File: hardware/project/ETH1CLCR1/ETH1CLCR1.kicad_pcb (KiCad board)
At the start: 6 copper layers, 160 x 100 mm, 680 parts, among them J1101 Conn_02x05, J1601 C64AC, J301 Conn_02x05, J302 Conn_02x01, J901 Conn_02x05, K1001 9012, K1002 9012, K1003 9012, K1004 9012, K1201 TQ2SA-5V, K1601 HE3621A0510, K1602 HE3621A0510, K1603 HE3621A0510, K1604 HE3621A0510, K1605 HE3621A0510, K1606 HE3621A0510, Q1001 MMBT4401L, Q1002 MMBT4403L, Q1003 BC847W, Q1004 BC847W, Q1005 BC847W, Q1006 BC847W, Q1201 2N2218A, Q1202 BC847W, Q1203 2N2904A, Q1204 BC847W, Q1501 BC847, Q1502 BC847, Q1503 BC847, Q1504 BC847, Q501 IRFR5410, U1001 TL072, U1002 LT1468, U1003 AQY212GS, U1004 AD5293BRUZ-20, U1101 STM32H743ZI, U1102 24LC08B-E/MS, U1201 AQY212GS, U1202 AQY212GS, U1203 AD5293BRUZ-20, U1204 TL072, U1205 AQY212GS, U1206 AQY212GS, U1207 AQY212GS, U1208 AQY212GS, U1209 AQY212GS, U1210 AQY212GS, U1211 AQY212GS, U1212 AQY212GS, U1213 HA3-2525-5Z, U1214 AQY212GS, U1215 AQY212GS, U1301 AQY212GS, U1302 TL072, U1303 AQY212GS, U1304 TL072, U1305 AQY212GS, U1306 AQY212GS, U1307 TL071, U1308 AQY212GS, U1309 TL072, U1310 AQY212GS, U1311 AQY212GS, U1312 TL072, U1313 AQY212GS, U1314 AQY212GS, U1315 TL071, U1316 AQY212GS, U1401 TL074, U1402 TL074, U1403 REF192, U1404 DAC7568ICPWR, U1501 INA159, U1502 ADG419BR, U1503 PGA103, U1504 OPA602, U1505 ADS8363, U1506 INA159, U1507 ADG419BR, U1508 PGA103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

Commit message: PCB layout
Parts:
- added C1218: C, Capacitor_SMD:C_0603_1608Metric_Pad1.05x0.95mm_HandSolder, B.Cu at (166.5, 51.8)
- C1206, C1208, C1209, C1210, C1211, C1212, C601, C602, C603, C604, C607, C613, C619, C620, C626, C901, C902, C903, C904, D1203, D1205, D1206, Q1202, R1216, R1217, R1219, R1220, R1222, R1223, R1224, R1225, R1226, R1227, R1229, R1230, R1231, R1234, R1238, R1239, R1242, R901, U1202, U1206, U1208, U1209, U1212, Y901: moved to B.Cu
- U602: value MC78M15CDTRKG -> MC7815BD2TG; footprint Package_TO_SOT_SMD:TO-252-2 -> Package_TO_SOT_SMD:TO-263-2
- U608: value MC79M15BDTRKG -> MC7915BD2TG; footprint Package_TO_SOT_SMD:TO-252-2 -> Package_TO_SOT_SMD:TO-263-2
- moved U1403 221.9 mm to (155.1, 98.7)
- moved Q1204 215.4 mm to (219.7, 79.6), turned to 270 degrees
- moved U1404 214.5 mm to (163.2, 98.7)
- moved U1212 212.4 mm to (186.1, 79.6), turned to 90 degrees
- moved K1201 211.7 mm to (199.5, 74.7), turned to 270 degrees
- moved C1206 207.4 mm to (193.2, 79.6), turned to 270 degrees
- moved U1207 206.9 mm to (186.1, 74.2), turned to 270 degrees
- moved U1214 203.9 mm to (209.7, 78.1)
- moved U1402 202.7 mm to (179.7, 97.0)
- moved U1205 201.6 mm to (186.2, 68.7), turned to 270 degrees
- moved R1214 200.8 mm to (190.8, 74.2), turned to 270 degrees
- moved R1216 200.3 mm to (209.7, 78.4), turned to 180 degrees
- moved R1215 198.5 mm to (181.4, 74.2), turned to 270 degrees
- moved U1210 196.4 mm to (215.6, 78.0)
- moved U1401 195.7 mm to (171.3, 97.0)
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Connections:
- C1006 pad 1: +12VF -> +15VF
- C1007 pad 1: +12VF -> +15VF
- C1008 pad 1: -12VF -> -15VF
- C1009 pad 1: -12VF -> -15VF
- U1001 pad 4: -12VF -> -15VF
- U1001 pad 8: +12VF -> +15VF

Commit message: PCB layout
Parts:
- removed the C801 at (161.1, 4.06)
- removed the C802 at (133.3, 29.8)
- removed the C818 at (136.1, 18.5)
- removed the C819 at (141.9, 15.2)
- removed the C820 at (141.9, 12.7)
- removed the C821 at (124.6, 30.6)
- removed the C822 at (152.4, 4.06)
- removed the C823 at (148.7, 6.57)
- removed the C824 at (131.9, 24.8)
- removed the C827 at (123.4, 33.1)
- removed the C828 at (144.2, 8.38)
- removed C834: 100n, Capacitor_SMD:C_0603_1608Metric_Pad1.05x0.95mm_HandSolder
- removed the R814 at (163.7, 11.6)
- removed the R820 at (129.0, 27.7)
- removed the R821 at (166.1, 6.57)
- removed the R824 at (165.5, 1.55)
- removed the R825 at (157.4, 9.08)
- removed the R826 at (137.7, 29.0)
- removed the R827 at (149.1, 16.6)
- removed R828, R829: 6k81, Resistor_SMD:R_0603_1608Metric_Pad1.05x0.95mm_HandSolder
- removed R830: 70k, Resistor_SMD:R_0603_1608Metric_Pad1.05x0.95mm_HandSolder
- removed R832: 237k, Resistor_SMD:R_0603_1608Metric_Pad1.05x0.95mm_HandSolder
- removed R833, R834, R835, R837, R841, R842, R845, R846: 10k, Resistor_SMD:R_0603_1608Metric_Pad1.05x0.95mm_HandSolder
- removed the U809 at (112.5, 17.0)
- removed U812: DG408DY, Package_SO:TSSOP-16_4.4x5mm_P0.65mm
- removed U813, U817: TL072, Package_SO:SOIC-8_3.9x4.9mm_P1.27mm
- removed U814: ADS7818, Package_SO:MSOP-8_3x3mm_P0.65mm
- removed U816: TXB0104PW, Package_SO:TSSOP-14_4.4x5mm_P0.65mm
- added C832: C, Capacitor_SMD:C_0603_1608Metric_Pad1.05x0.95mm_HandSolder, B.Cu at (147.4, 55.4)
- C1001, C1011, C1201, C1213, C1214, C1215, C1216, C1217, C1405, C1419, D1001, D1002, D1005, D1006, D1007, D1008, D1204, D1210, D1211, D1212, D1303, D801, Q1003, Q1004, Q1005, Q1006, R1003, R1006, R1023, R1203, R1204, R1206, R1208, R1209, R1212, R1213, R1233, R1236, R1237, R1240, R1241, U1003, U1004, U1303, U1307, U1308, U1315, U1316, U1504, U1509, U902: moved to B.Cu
- C1406: footprint Capacitor_SMD:C_0805_2012Metric_Pad1.15x1.40mm_HandSolder -> Capacitor_SMD:C_0603_1608Metric_Pad1.05x0.95mm_HandSolder; moved to B.Cu
- C801: renamed from C829; moved to B.Cu
- C802: renamed from C814; moved to B.Cu
- C803: renamed from C830; moved to B.Cu
- C804: renamed from C831; moved to B.Cu
- C805: renamed from C815; moved to B.Cu
- C806: renamed from C832; moved to B.Cu
- C807: renamed from C833; moved to B.Cu
- C808: renamed from C835; moved to B.Cu
- C809: renamed from C836; moved to B.Cu
- C811: renamed from C837; moved to B.Cu
- C815: renamed from C838; moved to B.Cu
- C816: renamed from C813; moved to B.Cu
- C819: renamed from C805; moved to B.Cu
- C821: renamed from C806; moved to B.Cu
- C822: renamed from C839; moved to B.Cu
- C824: renamed from C807; moved to B.Cu
- C825: renamed from C840; moved to B.Cu
- C827: renamed from C841; moved to B.Cu
- D1003, D1004: footprint Diode_SMD:D_SMA_Handsoldering -> Diode_SMD:D_SMA; moved to B.Cu
- R801: renamed from R822; moved to B.Cu
- R805: renamed from R823; moved to B.Cu
- R806: renamed from R813; moved to B.Cu
- R822: renamed from R808; moved to B.Cu
- R823: renamed from R803; moved to B.Cu
- R824: renamed from R804; moved to B.Cu
- R825: renamed from R809; moved to B.Cu
- R827: renamed from R801; value 10k -> R
- U803: renamed from U808; footprint Package_TO_SOT_SMD:SOT-353_SC-70-5_Handsoldering -> Package_TO_SOT_SMD:SOT-353_SC-70-5
- moved U1310 258.3 mm to (134.0, 101.7)
- moved U1311 247.3 mm to (134.0, 92.5)
- moved RV1303 243.4 mm to (172.1, 87.2), turned to 90 degrees
- moved U1309 237.3 mm to (163.8, 87.2)
- moved U1301 237.0 mm to (159.5, 93.5), turned to 270 degrees
- moved RV1302 233.4 mm to (172.1, 80.5), turned to 90 degrees
- moved U1306 232.7 mm to (169.3, 93.5), turned to 270 degrees
- moved U1308 231.4 mm to (169.3, 93.5), turned to 90 degrees
- moved RV1301 223.9 mm to (163.8, 73.2), turned to 180 degrees
- moved U1314 223.0 mm to (179.2, 93.3), turned to 270 degrees
- moved U1302 221.4 mm to (163.8, 80.6)
- moved U1304 220.1 mm to (179.8, 87.4)
- moved U1305 218.7 mm to (156.8, 86.2)
- moved U1303 216.4 mm to (159.5, 93.5), turned to 90 degrees
- moved C1406 215.1 mm to (156.5, 102.0), turned to 90 degrees
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- renumbered C816 to C810, C825 to C812, C817 to C813, C804 to C814, C826 to C817, C809 to C818, C810 to C820, C811 to C823, C812 to C826, C808 to C828, C842 to C829, C843 to C830, C803 to C831, R840 to R802, R836 to R803, R843 to R804, R815 to R807, R816 to R808, R806 to R809, R817 to R810, R818 to R811, R831 to R812, R812 to R813, R838 to R814, R844 to R815, R839 to R816, R810 to R817, R819 to R818, R811 to R819, R807 to R820, R802 to R821, R805 to R826, U807 to U801, U810 to U802, U815 to U804, U811 to U806, U804 to U807, U801 to U808, U802 to U809, U803 to U810, U806 to U811
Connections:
- C812 pad 1: Net-(C825-Pad1) -> Net-(C812-Pad1)
- C817 pad 2: Net-(C826-Pad2) -> Net-(C817-Pad2)
- R812 pad 1: Net-(C825-Pad1) -> Net-(C812-Pad1)
- R814 pad 1: Net-(C826-Pad2) -> Net-(C817-Pad2)
- R815 pad 1: Net-(C826-Pad2) -> Net-(C817-Pad2)
- R816 pad 2: Net-(C826-Pad2) -> Net-(C817-Pad2)
- R827 pad 1: /FGEN/MEAS_OUT -> AGNDF
- U806 pad 5: Net-(C823-Pad1) -> Net-(C812-Pad1)
- U806 pad 6: Net-(C819-Pad1) (its old number) -> Net-(C817-Pad2)
- U806 pad 7: Net-(C819-Pad1) (its old number) -> /FGEN/V_OFFSET
- U901 pad 11: /FGEN/DDS_MEAS_DATA -> (no net)
- U901 pad 29: /FGEN/DDS_MEAS_CLK -> (no net)
- U901 pad 38: /FGEN/DDS_MEAS_A0 -> (no net)
- U901 pad 39: /FGEN/DDS_MEAS_A1 -> (no net)
- U901 pad 40: /FGEN/DDS_MEAS_A2 -> (no net)
- U901 pad 62: /FGEN/DDS_MEAS_CONV -> (no net)

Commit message: PCB layout
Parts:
- added C832: 100n, Capacitor_SMD:C_0603_1608Metric_Pad1.05x0.95mm_HandSolder, B.Cu at (156.6, 62.7)
- added C833: 100n, Capacitor_SMD:C_0603_1608Metric_Pad1.05x0.95mm_HandSolder, B.Cu at (156.6, 60.3)
- added C835: 100n, Capacitor_SMD:C_0603_1608Metric_Pad1.05x0.95mm_HandSolder, F.Cu at (138.9, 65.9)
- C1003, C1004, C1005, C1006, C1007, C1008, C1009, C1010, C1301, C1302, C1304, C1305, C1306, C1307, C1401, C1411, C1417, C1418, C1420, C1421, C810, C812, C813, C817, C829, C830, C905, C906, C907, C908, C909, C910, C911, R1005, R1008, R1014, R1015, R1016, R1017, R1018, R1019, R1020, R1021, R1022, R1301, R1303, R1304, R1305, R1306, R1307, R1308, R1309, R1310, R1311, R1312, R1313, R1315, R1317, R1318, R1319, R1320, R1321, R1323, R1324, R1325, R1326, R1327, R1328, R1329, R1330, R1331, R1332, R1333, R1334, R1335, R1336, R1337, R1338, R1340, R1343, R1344, R1345, R1346, R1347, R1401, R1403, R1405, R1407, R1408, R1409, R1411, R1413, R1415, R1416, R1417, R1419, R1423, R1426, R1428, R802, R803, R804, R807, R808, R809, R810, R811, R812, R814, R815, R816, R818, R826, R827, R902, R903, R904: moved to B.Cu
- moved R1316 246.6 mm to (164.6, 93.1), turned to 270 degrees
- moved R1302 245.9 mm to (154.2, 93.1), turned to 90 degrees
- moved R1332 244.2 mm to (163.6, 86.4), turned to 90 degrees
- moved R1306 243.6 mm to (154.2, 93.1), turned to 90 degrees
- moved R1325 242.8 mm to (161.7, 88.9), turned to 180 degrees
- moved R1334 242.5 mm to (132.5, 103.8), turned to 180 degrees
- moved R1330 239.0 mm to (171.1, 86.5)
- moved R1326 237.2 mm to (160.8, 86.4), turned to 90 degrees
- moved C1304 237.0 mm to (165.2, 88.9)
- moved R1317 236.8 mm to (174.5, 88.9), turned to 180 degrees
- moved R1305 235.8 mm to (185.0, 86.9), turned to 90 degrees
- moved R1336 235.1 mm to (157.1, 89.2), turned to 180 degrees
- moved R1340 231.9 mm to (185.0, 83.4), turned to 270 degrees
- moved R1329 231.0 mm to (168.5, 87.6), turned to 270 degrees
- moved R1327 229.7 mm to (132.5, 95.1), turned to 180 degrees
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- renumbered C832 to C834
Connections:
- R1020 pad 1: /MCU2/SR10CTR -> /FGEN Buffer/SR10KCTR
- R1021 pad 1: /MCU2/FB_CAP -> /FGEN Buffer/SR100CTR
- R1022 pad 1: /MCU2/SR10KCTR -> /FGEN Buffer/SR1KCTR
- R1023 pad 1: /MCU2/SR100CTR -> /FGEN Buffer/SR10CTR
- U1101 pad 118: /MCU2/SR10KCTR -> /FGEN Buffer/SR10KCTR
- U1101 pad 119: /FGEN Buffer/FB_CAP -> /FGEN Buffer/SR1KCTR
- U1101 pad 122: /MCU2/SR100CTR -> /FGEN Buffer/SR100CTR
- U1101 pad 123: /MCU2/SR10CTR -> /FGEN Buffer/SR10CTR
- U1101 pad 124: /MCU2/FB_CAP -> /FGEN Buffer/FB_CAP

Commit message: Redesinged ADC schematic.
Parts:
- C1407, C1415, R1425: moved to B.Cu
- R1223: value 90k -> 90k/.01%
- R1234, R1237: value 2R7/.25W -> 2R7
- moved C1402 264.9 mm to (162.5, 144.5)
- moved C1408 264.9 mm to (153.8, 158.6)
- moved C1412 264.9 mm to (149.4, 159.2)
- moved C1414 264.9 mm to (145.7, 164.2)
- moved R1410 264.9 mm to (171.4, 149.5)
- moved R1418 264.9 mm to (166.8, 159.5)
- moved R1421 264.9 mm to (167.5, 162.1)
- moved R1422 264.9 mm to (171.2, 159.5)
- moved R1424 264.9 mm to (152.1, 160.8)
- moved R1402 230.3 mm to (158.7, 107.3)
- moved C1407 223.4 mm to (163.8, 104.4), turned to 270 degrees
- moved R1425 213.0 mm to (166.9, 98.0), turned to 90 degrees
- moved C1415 205.8 mm to (168.4, 98.0), turned to 90 degrees
- moved R1417 16.6 mm to (168.4, 104.4), turned to 270 degrees
- moved C1411 14.7 mm to (166.9, 104.4), turned to 270 degrees
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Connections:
- C1201 pad 2: Net-(C1201-Pad2) -> /Connector/LCUR
- C1202 pad 1: Net-(C1201-Pad2) -> /Connector/LCUR
- R1202 pad 2: Net-(C1201-Pad2) -> /Connector/LCUR
- R1207 pad 2: Net-(C1201-Pad2) -> /Connector/LCUR
- R1214 pad 2: Net-(C1201-Pad2) -> /Connector/LCUR
- R1218 pad 2: Net-(C1201-Pad2) -> /Connector/LCUR

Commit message: Redesigned the power supply, added humidy+temp. sensor.
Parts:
- removed the C1503 at (223.5, -91.6)
- removed the C1509 at (214.0, -70.5)
- removed the C1510 at (219.0, -91.3)
- removed the C1511 at (218.4, -74.0)
- removed the C1512 at (196.3, -69.0)
- removed the C1513 at (218.4, -76.5)
- removed the C1514 at (204.8, -77.6)
- removed the C1515 at (214.0, -73.0)
- removed the C1516 at (214.2, -88.4)
- removed the C1517 at (226.0, -86.5)
- removed the C1518 at (196.3, -72.0)
- removed the C1519 at (209.6, -68.3)
- removed the C1520 at (214.2, -91.3)
- removed the C601 at (99.3, 110.7)
- removed the C602 at (105.7, 134.2)
- removed the C603 at (97.9, 134.2)
- removed the C604 at (103.0, 100.6)
- removed the C607 at (94.2, 110.7)
- removed the C701 at (161.4, 121.8)
- removed the C702 at (154.4, 121.8)
- removed L601: 7448013501, ETH1CLCR1:7448013501
- removed the R1506 at (213.8, -78.1)
- removed the R1508 at (217.3, -81.6)
- removed R1509, R1510: 0, Resistor_SMD:R_0603_1608Metric_Pad1.05x0.95mm_HandSolder
- removed R1511: 100, Resistor_SMD:R_0603_1608Metric_Pad1.05x0.95mm_HandSolder
- removed the U1501 at (147.1, 105.8)
- removed the U1505 at (139.2, 103.6)
- removed the U1506 at (147.1, 102.0)
- removed the U1507 at (138.9, 90.7)
- removed the U601 at (96.8, 110.7)
- removed the U701 at (157.9, 120.0)
- added C1101: 1u, Capacitor_SMD:C_0603_1608Metric_Pad1.05x0.95mm_HandSolder, F.Cu at (119.8, 152.8)
- added C1102: 100n, Capacitor_SMD:C_0603_1608Metric_Pad1.05x0.95mm_HandSolder, F.Cu at (128.3, 148.1)
- added C1103: 1u, Capacitor_SMD:C_0603_1608Metric_Pad1.05x0.95mm_HandSolder, F.Cu at (151.4, 151.9)
- added C1104: 1u, Capacitor_SMD:C_0603_1608Metric_Pad1.05x0.95mm_HandSolder, F.Cu at (114.0, 159.2)
- added C1105: 1u, Capacitor_SMD:C_0603_1608Metric_Pad1.05x0.95mm_HandSolder, F.Cu at (151.4, 154.4)
- added C1106: 1u, Capacitor_SMD:C_0603_1608Metric_Pad1.05x0.95mm_HandSolder, F.Cu at (114.0, 161.7)
- added C1107: 1u, Capacitor_SMD:C_0603_1608Metric_Pad1.05x0.95mm_HandSolder, F.Cu at (118.4, 159.2)
- added C1108: 3300p, Capacitor_SMD:C_0603_1608Metric_Pad1.05x0.95mm_HandSolder, F.Cu at (118.4, 161.7)
- added C1109: 3300p, Capacitor_SMD:C_0603_1608Metric_Pad1.05x0.95mm_HandSolder, F.Cu at (122.7, 157.8)
- added C1110: 100n, Capacitor_SMD:C_0603_1608Metric_Pad1.05x0.95mm_HandSolder, F.Cu at (111.9, 166.8)
- added C1111: 100n, Capacitor_SMD:C_0603_1608Metric_Pad1.05x0.95mm_HandSolder, F.Cu at (133.6, 163.2)
- added C1112: 100n, Capacitor_SMD:C_0603_1608Metric_Pad1.05x0.95mm_HandSolder, F.Cu at (140.1, 158.2)
- added C1113: 100n, Capacitor_SMD:C_0603_1608Metric_Pad1.05x0.95mm_HandSolder, F.Cu at (131.4, 158.2)
- added C1114: 100n, Capacitor_SMD:C_0603_1608Metric_Pad1.05x0.95mm_HandSolder, F.Cu at (119.8, 155.3)
- added C1116: 1n, Capacitor_SMD:C_0603_1608Metric_Pad1.05x0.95mm_HandSolder, F.Cu at (116.2, 164.2)
- added C1117: 100n, Capacitor_SMD:C_0603_1608Metric_Pad1.05x0.95mm_HandSolder, F.Cu at (124.2, 152.8)
- added C1118: 100n, Capacitor_SMD:C_0603_1608Metric_Pad1.05x0.95mm_HandSolder, F.Cu at (111.9, 164.2)
- added C1119: 100n, Capacitor_SMD:C_0603_1608Metric_Pad1.05x0.95mm_HandSolder, F.Cu at (129.3, 165.7)
- added C1120: 100n, Capacitor_SMD:C_0603_1608Metric_Pad1.05x0.95mm_HandSolder, F.Cu at (132.6, 148.1)
- added C322: 100n, Capacitor_SMD:C_0603_1608Metric_Pad1.05x0.95mm_HandSolder, F.Cu at (99.3, 100.5)
- added R1101: 100, Resistor_SMD:R_0603_1608Metric_Pad1.05x0.95mm_HandSolder, F.Cu at (128.5, 150.6)
- added R1102: 100, Resistor_SMD:R_0603_1608Metric_Pad1.05x0.95mm_HandSolder, F.Cu at (128.5, 153.1)
- added R1103: 1k, Resistor_SMD:R_0603_1608Metric_Pad1.05x0.95mm_HandSolder, F.Cu at (132.9, 150.6)
- added R1104: 1k, Resistor_SMD:R_0603_1608Metric_Pad1.05x0.95mm_HandSolder, F.Cu at (122.7, 160.3)
- added R1105: 100, Resistor_SMD:R_0603_1608Metric_Pad1.05x0.95mm_HandSolder, F.Cu at (137.2, 153.1)
- added R1106: 100, Resistor_SMD:R_0603_1608Metric_Pad1.05x0.95mm_HandSolder, F.Cu at (128.5, 155.7)
- added R1107: 100, Resistor_SMD:R_0603_1608Metric_Pad1.05x0.95mm_HandSolder, F.Cu at (131.4, 160.7)
- added R1108: 100, Resistor_SMD:R_0603_1608Metric_Pad1.05x0.95mm_HandSolder, F.Cu at (137.0, 148.1)
- added R1109: 50, Resistor_SMD:R_0603_1608Metric_Pad1.05x0.95mm_HandSolder, F.Cu at (137.2, 155.7)
- added R1110: 50, Resistor_SMD:R_0603_1608Metric_Pad1.05x0.95mm_HandSolder, F.Cu at (129.3, 163.2)
- added R1111: 50, Resistor_SMD:R_0603_1608Metric_Pad1.05x0.95mm_HandSolder, F.Cu at (135.8, 158.2)
- added R1112: 50, Resistor_SMD:R_0603_1608Metric_Pad1.05x0.95mm_HandSolder, F.Cu at (135.8, 160.7)
- added R1113: 52k3, Resistor_SMD:R_0603_1608Metric_Pad1.05x0.95mm_HandSolder, F.Cu at (124.2, 155.3)
- added R1115: 52k3, Resistor_SMD:R_0603_1608Metric_Pad1.05x0.95mm_HandSolder, F.Cu at (124.9, 165.7)
- added R1116: 100, Resistor_SMD:R_0603_1608Metric_Pad1.05x0.95mm_HandSolder, F.Cu at (116.2, 166.8)
- added R1117: 12k, Resistor_SMD:R_0603_1608Metric_Pad1.05x0.95mm_HandSolder, F.Cu at (120.6, 164.2)
- added R1118: 12k, Resistor_SMD:R_0603_1608Metric_Pad1.05x0.95mm_HandSolder, F.Cu at (132.9, 153.1)
- added R1119: 12k, Resistor_SMD:R_0603_1608Metric_Pad1.05x0.95mm_HandSolder, F.Cu at (137.2, 150.6)
- added R1120: 10k, Resistor_SMD:R_0603_1608Metric_Pad1.05x0.95mm_HandSolder, F.Cu at (120.6, 166.8)
- added R1121: 12k, Resistor_SMD:R_0603_1608Metric_Pad1.05x0.95mm_HandSolder, F.Cu at (127.1, 158.2)
- added R1122: 10k, Resistor_SMD:R_0603_1608Metric_Pad1.05x0.95mm_HandSolder, F.Cu at (127.1, 160.7)
- added R1123: 52k3, Resistor_SMD:R_0603_1608Metric_Pad1.05x0.95mm_HandSolder, F.Cu at (132.9, 155.7)
- added R1124: 52k3, Resistor_SMD:R_0603_1608Metric_Pad1.05x0.95mm_HandSolder, F.Cu at (124.9, 163.2)
- added U1101: ADG419BR, Package_SO:SOIC-8_3.9x4.9mm_P1.27mm, F.Cu at (87.4, 167.8)
- added U1103: AD8606-2-MSOP, Package_SO:MSOP-8_3x3mm_P0.65mm, F.Cu at (112.9, 173.6)
- added U1104: AD7380, Package_CSP:LFCSP-16-1EP_3x3mm_P0.5mm_EP1.6x1.6mm, F.Cu at (140.1, 91.3)
- added U1105: AD8605, Package_TO_SOT_SMD:SOT-23-5_HandSoldering, F.Cu at (119.3, 172.2)
- added U1106: AD8605, Package_TO_SOT_SMD:SOT-23-5_HandSoldering, F.Cu at (119.3, 177.2)
- added U1107: LT6350, Package_SO:MSOP-8_3x3mm_P0.65mm, F.Cu at (107.3, 172.2)
- added U1108: LT6350, Package_SO:MSOP-8_3x3mm_P0.65mm, F.Cu at (107.3, 176.7)
- added U303: HDC1080, Package_SON:Texas_PWSON-N6, F.Cu at (94.6, 101.6)
- C815: renamed from C1201; moved to F.Cu
- R814: renamed from R1213; moved to F.Cu
- R819: renamed from R1203; moved to F.Cu
- R824: renamed from R1223; moved to F.Cu
- R829: renamed from R1219; moved to F.Cu
- R830: renamed from R1224; moved to F.Cu
- R927: renamed from R1316; moved to B.Cu
- R929: renamed from R1339; moved to B.Cu
- U1109: renamed from U1504; moved to F.Cu
- U1110: renamed from U1509; moved to F.Cu
- U1509: renamed from U605; footprint Package_TO_SOT_SMD:SOT-223-3_TabPin2 -> Package_TO_SOT_SMD:TO-252-2
- U1510: renamed from U606; footprint Package_TO_SOT_SMD:SOT-223-3_TabPin2 -> Package_TO_SOT_SMD:TO-252-2
- U1511: renamed from U610; footprint Package_TO_SOT_SMD:SOT-223-3_TabPin2 -> Package_TO_SOT_SMD:TO-252-2
- U703: renamed from U1003; moved to F.Cu
- U704: renamed from U1004; moved to F.Cu
- U905: renamed from U1307; moved to F.Cu
- U906: renamed from U1315; moved to F.Cu
- U908: renamed from U1303; moved to F.Cu
- U910: renamed from U1308; moved to F.Cu
- U912: renamed from U1316; moved to F.Cu
- moved C1115 273.2 mm to (128.4, 186.4)
- moved C1121 273.2 mm to (132.8, 181.4)
- moved C1122 273.2 mm to (124.1, 182.4)
- moved C1123 273.2 mm to (132.8, 183.9)
- moved C1124 273.2 mm to (140.4, 171.4)
- moved C1125 273.2 mm to (140.4, 173.9)
- moved C1126 273.2 mm to (136.1, 173.9)
- moved R1114 273.2 mm to (138.0, 168.9)
- moved R1125 273.2 mm to (131.7, 173.9)
- moved R1126 273.2 mm to (119.7, 187.1)
- moved R1127 273.2 mm to (119.7, 184.6)
- moved R1128 273.2 mm to (133.6, 168.9)
- moved R1129 273.2 mm to (138.0, 166.4)
- moved R1130 273.2 mm to (136.9, 176.4)
- moved R1131 273.2 mm to (127.4, 173.9)
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- renumbered C1405 to C1001, C1417 to C1002, C1418 to C1003, C1406 to C1004, C1419 to C1005, C1420 to C1006, C1421 to C1007, C1401 to C1008, C1407 to C1009, C1411 to C1010, C1415 to C1011, C1403 to C1012, C1409 to C1013, C1413 to C1014, C1416 to C1015, C1402 to C1016, C1408 to C1017, C1412 to C1018, C1404 to C1019, C1410 to C1020, C1414 to C1021, C1501 to C1115, C1505 to C1121, C1507 to C1122, C1502 to C1123, C1504 to C1124, C1506 to C1125, C1508 to C1126, C1108 to C1301, C1101 to C1302, C1109 to C1303, C1102 to C1304, C1110 to C1305, C1103 to C1306, C1104 to C1307, C1111 to C1308, C1112 to C1309, C1106 to C1310, C1113 to C1311, C1114 to C1312, C1115 to C1313, C1116 to C1314, C1117 to C1315, C1118 to C1316, C1119 to C1317, C1107 to C1318, C1105 to C1319, C801 to C1401, C802 to C1402, C803 to C1403, C804 to C1404, C805 to C1405, C806 to C1406, C807 to C1407, C808 to C1408, C809 to C1409, C810 to C1410, C811 to C1411, C812 to C1412, C813 to C1413, C814 to C1414, C815 to C1415, C816 to C1416, C817 to C1417, C818 to C1418, C819 to C1419, C820 to C1420, C821 to C1421, C822 to C1422, C823 to C1423, C824 to C1424, C825 to C1425, C826 to C1426, C827 to C1427, C828 to C1428, C829 to C1429, C830 to C1430, C831 to C1431, C832 to C1432, C833 to C1433, C835 to C1434, C834 to C1435, C608 to C1501, C627 to C1502, C614 to C1503, C632 to C1504, C605 to C1505, C621 to C1506, C609 to C1507, C628 to C1508, C610 to C1509, C629 to C1510, C611 to C1511, C630 to C1512, C612 to C1513, C631 to C1514, C606 to C1515, C622 to C1516, C615 to C1517, C616 to C1518, C623 to C1519, C617 to C1520, C624 to C1521, C618 to C1522, C619 to C1523, C625 to C1524, C613 to C1525, C620 to C1526, C626 to C1527, C213 to C201, C201 to C202, C208 to C203, C214 to C204, C202 to C205, C209 to C206, C203 to C207, C204 to C208, C205 to C209, C206 to C210, C207 to C211, C210 to C212, C212 to C213, C211 to C214, C307 to C301, C308 to C302, C301 to C303, C309 to C304, C302 to C305, C310 to C306, C303 to C307, C311 to C308, C304 to C309, C312 to C310, C306 to C311, C313 to C312, C314 to C313, C315 to C314, C316 to C315, C317 to C316, C318 to C317, C319 to C318, C320 to C319, C321 to C320, C305 to C321, C407 to C401, C408 to C402, C401 to C403, C402 to C404, C403 to C405, C404 to C406, C405 to C407, C406 to C408, C905 to C601, C906 to C602, C907 to C603, C908 to C604, C909 to C605, C910 to C606, C911 to C607, C903 to C608, C904 to C609, C901 to C610, C902 to C611, C1003 to C701, C1010 to C702, C1004 to C703, C1011 to C704, C1002 to C705, C1006 to C706, C1007 to C707, C1008 to C708, C1009 to C709, C1001 to C710, C1005 to C711, C1212 to C801, C1213 to C802, C1214 to C803, C1204 to C804, C1208 to C805, C1209 to C806, C1215 to C807, C1216 to C808, C1217 to C809, C1205 to C810, C1211 to C811, C1218 to C812, C1203 to C813, C1202 to C814, C1206 to C816, C1207 to C817, C1210 to C818, C1306 to C901, C1302 to C902, C1307 to C903, C1303 to C904, C1305 to C905, C1304 to C906, C1301 to C907, D801 to D1401, D602 to D1501, D601 to D1502, D402 to D401, D401 to D402, D502 to D501, D503 to D502, D501 to D503, D1005 to D701, D1006 to D702, D1007 to D703, D1008 to D704, D1001 to D705, D1002 to D706, D1003 to D707, D1004 to D708, D1201 to D801, D1207 to D802, D1202 to D803, D1208 to D804, D1209 to D805, D1204 to D806, D1212 to D807, D1205 to D808, D1210 to D809, D1206 to D810, D1211 to D811, D1203 to D812, D1303 to D901, D1301 to D902, D1302 to D903, FB1101 to FB1301, J1601 to J1201, J1101 to J1301, J302 to J301, J301 to J302, J901 to J601, K1601 to K1201, K1602 to K1202, K1603 to K1203, K1604 to K1204, K1605 to K1205, K1606 to K1206, K1001 to K701, K1003 to K702, K1002 to K703, K1004 to K704, K1201 to K801, L801 to L1401, L802 to L1402, L803 to L1403, L602 to L1501, L604 to L1502, L603 to L1503, L605 to L1504, Q1501 to Q1101, Q1503 to Q1102, Q1502 to Q1103, Q1504 to Q1104, Q1003 to Q701, Q1005 to Q702, Q1004 to Q703, Q1006 to Q704, Q1001 to Q705, Q1002 to Q706, Q1204 to Q801, Q1201 to Q802, Q1203 to Q803, Q1202 to Q804, R1401 to R1001, R1409 to R1002, R1417 to R1003, R1425 to R1004, R1403 to R1005, R1407 to R1006, R1411 to R1007, R1415 to R1008, R1419 to R1009, R1423 to R1010, R1426 to R1011, R1428 to R1012, R1404 to R1013, R1412 to R1014, R1420 to R1015, R1427 to R1016, R1402 to R1017, R1410 to R1018, R1418 to R1019, R1405 to R1020, R1408 to R1021, R1413 to R1022, R1416 to R1023, R1421 to R1024, R1424 to R1025, R1406 to R1026, R1414 to R1027, R1422 to R1028, R1501 to R1114, R1503 to R1125, R1513 to R1126, R1504 to R1127, R1514 to R1128, R1505 to R1129, R1507 to R1130, R1515 to R1131, R1516 to R1132, R1517 to R1133, R1519 to R1134, R1502 to R1135, R1512 to R1136, R1518 to R1137, R1520 to R1138, R1103 to R1301, R1104 to R1302, R1102 to R1303, R1101 to R1304, R801 to R1401, R802 to R1402, R803 to R1403, R804 to R1404, R805 to R1405, R806 to R1406, R807 to R1407, R808 to R1408, R809 to R1409, R810 to R1410, R811 to R1411, R812 to R1412, R813 to R1413, R814 to R1414, R815 to R1415, R816 to R1416, R817 to R1417, R818 to R1418, R819 to R1419, R820 to R1420, R821 to R1421, R822 to R1422, R823 to R1423, R824 to R1424, R825 to R1425, R826 to R1426, R827 to R1427, R601 to R1501, R603 to R1502, R605 to R1503, R607 to R1504, R602 to R1505, R604 to R1506, R606 to R1507, R608 to R1508, R205 to R201, R206 to R202, R207 to R203, R208 to R204, R212 to R205, R217 to R206, R218 to R207, R219 to R208, R220 to R209, R221 to R210, R213 to R211, R209 to R212, R214 to R213, R215 to R214, R201 to R215, R202 to R216, R203 to R217, R204 to R218, R216 to R219, R210 to R220, R211 to R221, R306 to R301, R307 to R302, R308 to R303, R305 to R304, R301 to R305, R302 to R306, R304 to R307, R303 to R308, R406 to R401, R401 to R404, R404 to R405, R405 to R406, R903 to R601, R904 to R602, R902 to R603, R901 to R604, R1020 to R701, R1022 to R702, R1016 to R703, R1008 to R704, R1018 to R705, R1021 to R706, R1023 to R707, R1005 to R708, R1011 to R709, R1013 to R710, R1014 to R711, R1017 to R712, R1001 to R713, R1002 to R714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
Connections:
- C1115 pad 1: Net-(C1501-Pad1) -> Net-(C1115-Pad1)
- C1501 pad 1: +24VF -> +24VDD
- C1502 pad 1: +24VF -> +24VDD
- C1517 pad 1: +24VF -> +24VDD
- C1518 pad 1: +24VF -> +24VDD
- C1519 pad 1: +24VF -> +24VDD
- C201 pad 2: GND -> AGNDF
- C202 pad 2: GND -> AGNDF
- C203 pad 2: GND -> AGNDF
- C204 pad 2: GND -> AGNDF
- C205 pad 2: GND -> AGNDF
- C206 pad 2: GND -> AGNDF
- C207 pad 2: GND -> AGNDF
- C208 pad 2: GND -> AGNDF
- C209 pad 2: GND -> AGNDF
- C210 pad 2: GND -> AGNDF
- C211 pad 2: GND -> AGNDF
- C212 pad 2: GND -> AGNDF
- C213 pad 2: GND -> AGNDF
- C301 pad 2: GND -> AGNDF
- C302 pad 2: GND -> AGNDF
- C303 pad 2: GND -> AGNDF
- C304 pad 2: GND -> AGNDF
- C305 pad 2: GND -> AGNDF
- C306 pad 2: GND -> AGNDF
- C307 pad 2: GND -> AGNDF
- C308 pad 2: GND -> AGNDF
- C309 pad 2: GND -> AGNDF
- C310 pad 2: GND -> AGNDF
- C311 pad 2: GND -> AGNDF
- C312 pad 2: GND -> AGNDF
- C313 pad 2: GND -> AGNDF
- C314 pad 2: GND -> AGNDF
- C315 pad 2: GND -> AGNDF
- C316 pad 2: GND -> AGNDF
- C317 pad 2: GND -> AGNDF
- C318 pad 2: GND -> AGNDF
- C319 pad 2: GND -> AGNDF
- C320 pad 2: GND -> AGNDF
- C321 pad 2: GND -> AGNDF
- C401 pad 2: GND -> AGNDF
- C402 pad 2: GND -> AGNDF
- C403 pad 2: GND -> AGNDF
- C404 pad 2: GND -> AGNDF
- C501 pad 2: GND -> AGNDF
- C502 pad 2: GND -> AGNDF
- C503 pad 2: GND -> AGNDF
- C504 pad 2: GND -> AGNDF
- D501 pad 2: GND -> AGNDF
- D502 pad 1: GND -> AGNDF
- J1201 pad A27: GND -> AGNDF
- J1201 pad A28: GND -> AGNDF
- J1201 pad C27: GND -> AGNDF
- J1201 pad C28: GND -> AGNDF
- J301 pad 2: GND -> AGNDF
- J302 pad 3: GND -> AGNDF
- J302 pad 5: GND -> AGNDF
- L1501 pad 1: +24VF -> +24VDD
- L1502 pad 1: +24VF -> +24VDD
- L1503 pad 1: +24VF -> +24VDD
- L1504 pad 1: +24VF -> +24VDD
- R1114 pad 1: Net-(C1501-Pad1) -> Net-(R1113-Pad1)
- R1114 pad 2: Net-(R1501-Pad2) (its old number) -> Net-(C1115-Pad1)
- R1501 pad 1: +24VF -> +24VDD
- R1503 pad 1: +24VF -> +24VDD
- R203 pad 2: GND -> AGNDF
- R211 pad 2: GND -> AGNDF
- R212 pad 1: GND -> AGNDF
- R213 pad 2: GND -> AGNDF
- R214 pad 2: GND -> AGNDF
- R219 pad 2: GND -> AGNDF
- R307 pad 2: GND -> AGNDF
- U1302 pad 1: /Isolation/MCU2_SCLK -> /MCU1/MCU1_MCLK
- U1302 pad 3: /Isolation/MCU2_~SSS -> /MCU1/MCU1_~SS
- U1302 pad 35: /ADC/ADC_CONVST -> (no net)
- U1302 pad 36: /ADC/ADC_RD -> (no net)
- U1302 pad 37: /ADC/ADC_BUSY -> /ADC/ADC_~ALARM
- U1302 pad 4: /Isolation/MCU2_MISO -> /MCU1/MCU1_MISO
- U1302 pad 41: /ADC/ADC_CLOCK -> /ADC/ADC_SCLK
- U1302 pad 5: /Isolation/MCU2_MOSI -> /MCU1/MCU1_MOSI
- U1302 pad 7: /Isolation/MCU2_GPIO_OUT1 -> /MCU1/MCU1_GPIO_OUT1
- U1302 pad 8: /Isolation/MCU2_GPIO_OUT2 -> /MCU1/MCU1_GPIO_OUT2
- U1302 pad 9: /Isolation/MCU2_STATUS_IN -> /MCU1/MCU1_STATUS_IN
- U1501 pad 6: +24VF -> +24VDD
- U1502 pad 6: +24VF -> +24VDD
- U201 pad 25: GND -> AGNDF
- U301 pad 107: GND -> AGNDF
- U301 pad 120: GND -> AGNDF
- U301 pad 130: GND -> AGNDF
- U301 pad 16: GND -> AGNDF
- U301 pad 18: /Isolation/MCU1_~MSS -> /MCU1/MCU1_~SS
- U301 pad 19: /Isolation/MCU1_MCLK -> /MCU1/MCU1_MCLK
- U301 pad 20: /Isolation/MCU1_MISO -> /MCU1/MCU1_MISO
- U301 pad 21: /Isolation/MCU1_MOSI -> /MCU1/MCU1_MOSI
- U301 pad 22: /Isolation/MCU1_GPIO_OUT1 -> /MCU1/MCU1_GPIO_OUT1
- U301 pad 26: /Isolation/MCU1_GPIO_OUT2 -> /MCU1/MCU1_GPIO_OUT2
- U301 pad 28: /Isolation/MCU1_STATUS_IN -> /MCU1/MCU1_STATUS_IN
- U301 pad 31: GND -> AGNDF
- U301 pad 38: GND -> AGNDF
- U301 pad 51: GND -> AGNDF
- U301 pad 61: GND -> AGNDF
- U301 pad 83: GND -> AGNDF
- U301 pad 94: GND -> AGNDF
- U302 pad 1: GND -> AGNDF
- U302 pad 2: GND -> AGNDF
- U302 pad 3: GND -> AGNDF
- U302 pad 4: GND -> AGNDF
- U401 pad 7: GND -> AGNDF
- U402 pad 2: GND -> AGNDF
- U402 pad 8: GND -> AGNDF
- U501 pad 4: GND -> AGNDF
- U502 pad 2: GND -> AGNDF
- U503 pad 1: GND -> AGNDF

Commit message: PCB layout
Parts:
- added C712: 100n, Capacitor_SMD:C_0603_1608Metric_Pad1.05x0.95mm_HandSolder, B.Cu at (168.5, 66.2)
- added R1139: 499, Resistor_SMD:R_0603_1608Metric_Pad1.05x0.95mm_HandSolder, F.Cu at (106.5, 161.8)
- added R1140: 499, Resistor_SMD:R_0603_1608Metric_Pad1.05x0.95mm_HandSolder, F.Cu at (106.5, 164.3)
- added R309: 4k7, Resistor_SMD:R_0603_1608Metric_Pad1.05x0.95mm_HandSolder, F.Cu at (53.6, 109.0)
- added R310: 4k7, Resistor_SMD:R_0603_1608Metric_Pad1.05x0.95mm_HandSolder, F.Cu at (53.6, 111.5)
- C1418, R1420, U1403, U703: moved to B.Cu
- C1419, C1421, C1424, D705, D706, D901, R1406, R703, R708, R902, R905, R911, R919: moved to F.Cu
- R1506: value R -> 97k6
- R1508: value R -> 46k4
- R804, R805: value 21R5 -> 21R5/.5W; footprint Resistor_SMD:R_0603_1608Metric_Pad1.05x0.95mm_HandSolder -> Resistor_SMD:R_0805_2012Metric_Pad1.15x1.40mm_HandSolder
- moved C711 226.7 mm to (166.9, 72.8), turned to 180 degrees
- moved C707 226.5 mm to (168.1, 69.3)
- moved C709 223.3 mm to (165.6, 69.3)
- moved R709 187.2 mm to (149.9, 75.4), turned to 90 degrees
- moved U701 186.7 mm to (153.3, 69.8), turned to 0 degrees
- moved Q705 185.6 mm to (152.7, 75.4), turned to 0 degrees
- moved R710 184.8 mm to (156.3, 75.4), turned to 270 degrees
- moved Q706 183.2 mm to (159.1, 75.4), turned to 0 degrees
- moved RV903 183.0 mm to (144.9, 55.4)
- moved RV901 182.6 mm to (144.9, 45.2)
- moved D706 179.0 mm to (159.6, 71.5)
- moved D705 178.8 mm to (159.6, 68.3)
- moved RV701 177.1 mm to (144.9, 70.6), turned to 90 degrees
- moved R723 176.3 mm to (145.5, 70.6), turned to 180 degrees
- moved R711 168.1 mm to (161.3, 85.3), turned to 270 degrees
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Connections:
- U1107 pad 2: /ADC/VCM -> Net-(R1139-Pad1)
- U1108 pad 2: /ADC/VCM -> Net-(R1140-Pad1)
- U301 pad 10: (no net) -> /MCU1/SENS_SDA
- U301 pad 11: (no net) -> /MCU1/SENS_SCL
- U303 pad 1: (no net) -> /MCU1/SENS_SDA
- U303 pad 6: (no net) -> /MCU1/SENS_SCL

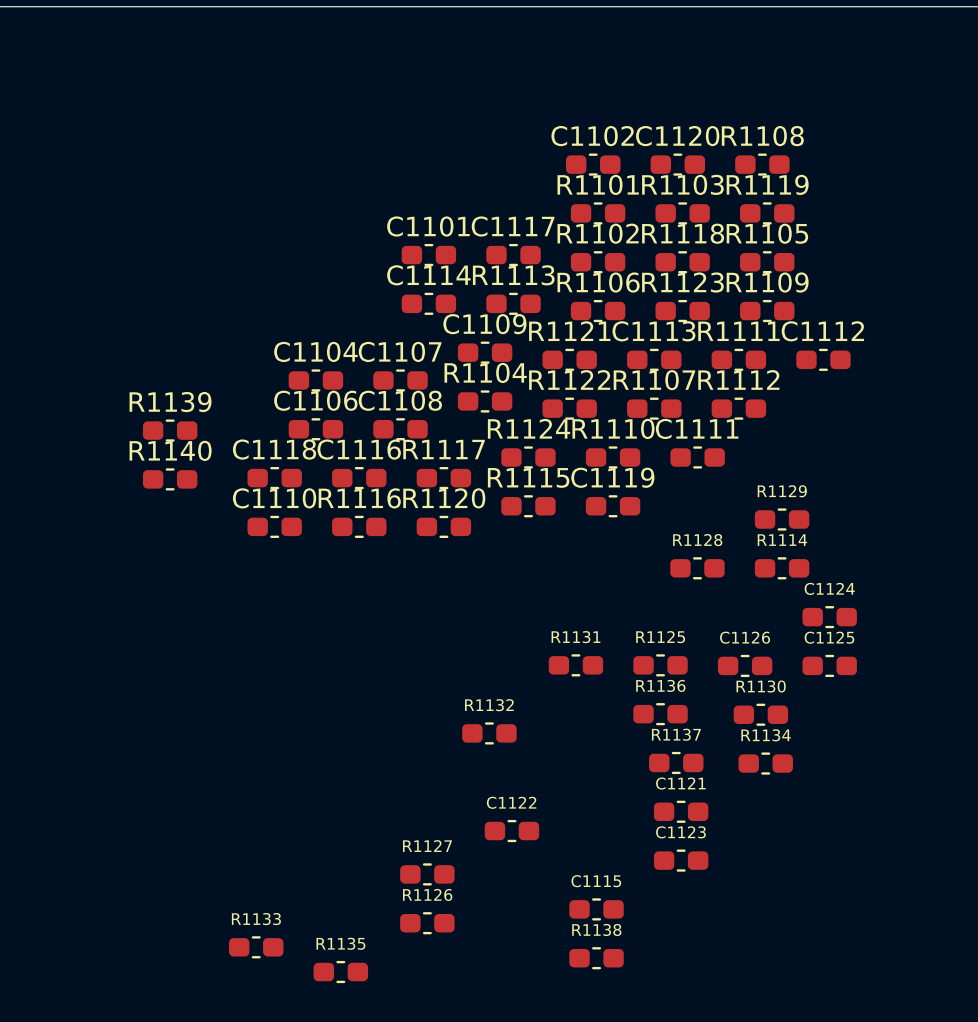
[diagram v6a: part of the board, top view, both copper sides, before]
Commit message: Fixed mistake in ADC schematic.
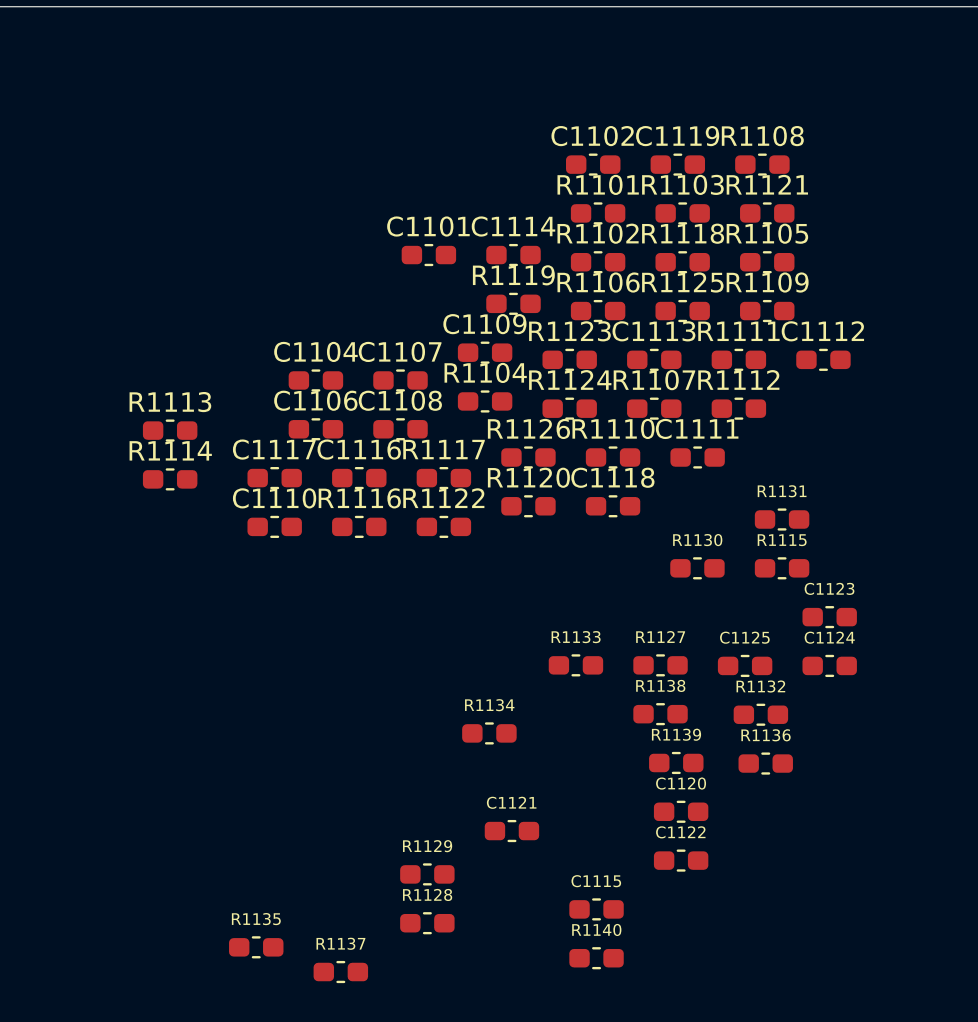
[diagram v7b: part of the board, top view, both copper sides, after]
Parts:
- removed the C1114 at (119.8, 155.3)
- renumbered C1117 to C1114, C1118 to C1117, C1119 to C1118, C1120 to C1119, C1121 to C1120, C1122 to C1121, C1123 to C1122, C1124 to C1123, C1125 to C1124, C1126 to C1125, R1139 to R1113, R1140 to R1114, R1114 to R1115, R1113 to R1119, R1115 to R1120, R1119 to R1121, R1120 to R1122, R1121 to R1123, R1122 to R1124, R1123 to R1125, R1124 to R1126, R1125 to R1127, R1126 to R1128, R1127 to R1129, R1128 to R1130, R1129 to R1131, R1130 to R1132, R1131 to R1133, R1132 to R1134, R1133 to R1135, R1134 to R1136, R1135 to R1137, R1136 to R1138, R1137 to R1139, R1138 to R1140
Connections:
- R1115 pad 1: Net-(R1113-Pad1) (its old number) -> Net-(R1115-Pad1)
- R1116 pad 1: Net-(R1115-Pad1) -> Net-(R1116-Pad1)
- R1117 pad 2: Net-(R1113-Pad1) (its old number) -> Net-(R1115-Pad1)
- R1118 pad 2: Net-(R1115-Pad1) -> Net-(R1116-Pad1)
- R1119 pad 1: Net-(R1113-Pad1) (its old number) -> Net-(R1117-Pad1)
- R1120 pad 1: Net-(R1115-Pad1) -> Net-(R1118-Pad1)
- U1103 pad 1: Net-(R1115-Pad1) -> Net-(R1116-Pad1)
- U1103 pad 7: Net-(R1113-Pad1) (its old number) -> Net-(R1115-Pad1)
